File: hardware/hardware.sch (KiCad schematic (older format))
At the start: 32 parts, among them J1 6P6C, J2 RJ45_LED_Shielded, Q1 BUK7M33-60EX, U1 Teensy4.1_DEV-16771, U2 LT1910, U3 OKI, U4 OKI-78SR-3.3_1.5-W36H-C, U5 OPAMP

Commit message: Footprints and layout work
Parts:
- C10, C11, C12, C13, C14, C15: footprint (none) -> Capacitor_SMD:C_0603_1608Metric_Pad1.08x0.95mm_HandSolder
- J2: footprint (none) -> MRDT_Connectors:RJ45_Teensy
- R2, R3, R4, R5: footprint (none) -> Resistor_SMD:R_0603_1608Metric_Pad0.98x0.95mm_HandSolder
- U5: footprint (none) -> Package_SO:SOIC-14_3.9x8.7mm_P1.27mm
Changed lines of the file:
@@
 F 0 "J2" V 750 4450 50  0000 L CNN
 F 1 "RJ45_LED_Shielded" V 850 4100 50  0000 L CNN
-F 2 "" V 1350 4575 50  0001 C CNN
+F 2 "MRDT_Connectors:RJ45_Teensy" V 1350 4575 50  0001 C CNN
 F 3 "~" V 1350 4575 50  0001 C CNN
 	1    1350 4550
@@
 F 0 "U5" H 7294 1796 50  0000 L CNN
 F 1 "OPAMP" H 7294 1705 50  0000 L CNN
-F 2 "" H 6950 1750 50  0001 C CNN
+F 2 "Package_SO:SOIC-14_3.9x8.7mm_P1.27mm" H 6950 1750 50  0001 C CNN
 F 3 "~" H 6950 1750 50  0001 C CNN
 	1    6950 1750
@@
 F 0 "R2" V 5893 1650 50  0000 C CNN
 F 1 "R" V 5984 1650 50  0000 C CNN
-F 2 "" V 6030 1650 50  0001 C CNN
+F 2 "Resistor_SMD:R_0603_1608Metric_Pad0.98x0.95mm_HandSolder" V 6030 1650 50  0001 C CNN
 F 3 "~" H 6100 1650 50  0001 C CNN
 	1    6100 1650
@@
 F 0 "R3" H 6420 2046 50  0000 L CNN
 F 1 "R" H 6420 1955 50  0000 L CNN
-F 2 "" V 6280 2000 50  0001 C CNN
+F 2 "Resistor_SMD:R_0603_1608Metric_Pad0.98x0.95mm_HandSolder" V 6280 2000 50  0001 C CNN
 F 3 "~" H 6350 2000 50  0001 C CNN
 	1    6350 2000
@@
 F 0 "R4" H 6620 1446 50  0000 L CNN
 F 1 "R" H 6620 1355 50  0000 L CNN
-F 2 "" V 6480 1400 50  0001 C CNN
+F 2 "Resistor_SMD:R_0603_1608Metric_Pad0.98x0.95mm_HandSolder" V 6480 1400 50  0001 C CNN
 F 3 "~" H 6550 1400 50  0001 C CNN
 	1    6550 1400
@@
 F 0 "R5" V 6893 2200 50  0000 C CNN
 F 1 "R" V 6984 2200 50  0000 C CNN
-F 2 "" V 7030 2200 50  0001 C CNN
+F 2 "Resistor_SMD:R_0603_1608Metric_Pad0.98x0.95mm_HandSolder" V 7030 2200 50  0001 C CNN
 F 3 "~" H 7100 2200 50  0001 C CNN
 	1    7100 2200
@@
 F 0 "C10" H 1335 1904 50  0000 R CNN
 F 1 "10uF" H 1335 1995 50  0000 R CNN
-F 2 "" H 1488 1800 50  0001 C CNN
+F 2 "Capacitor_SMD:C_0603_1608Metric_Pad1.08x0.95mm_HandSolder" H 1488 1800 50  0001 C CNN
 F 3 "~" H 1450 1950 50  0001 C CNN
 	1    1450 1950
@@
 F 0 "C13" H 935 1904 50  0000 R CNN
 F 1 "10uF" H 935 1995 50  0000 R CNN
-F 2 "" H 1088 1800 50  0001 C CNN
+F 2 "Capacitor_SMD:C_0603_1608Metric_Pad1.08x0.95mm_HandSolder" H 1088 1800 50  0001 C CNN
 F 3 "~" H 1050 1950 50  0001 C CNN
 	1    1050 1950
@@
 F 0 "C11" H 535 1904 50  0000 R CNN
 F 1 "10uF" H 535 1995 50  0000 R CNN
-F 2 "" H 688 1800 50  0001 C CNN
+F 2 "Capacitor_SMD:C_0603_1608Metric_Pad1.08x0.95mm_HandSolder" H 688 1800 50  0001 C CNN
 F 3 "~" H 650 1950 50  0001 C CNN
 	1    650  1950
@@
 F 0 "C15" H 1335 2304 50  0000 R CNN
 F 1 "10uF" H 1335 2395 50  0000 R CNN
-F 2 "" H 1488 2200 50  0001 C CNN
+F 2 "Capacitor_SMD:C_0603_1608Metric_Pad1.08x0.95mm_HandSolder" H 1488 2200 50  0001 C CNN
 F 3 "~" H 1450 2350 50  0001 C CNN
 	1    1450 2350
@@
 F 0 "C14" H 935 2304 50  0000 R CNN
 F 1 "10uF" H 935 2395 50  0000 R CNN
-F 2 "" H 1088 2200 50  0001 C CNN
+F 2 "Capacitor_SMD:C_0603_1608Metric_Pad1.08x0.95mm_HandSolder" H 1088 2200 50  0001 C CNN
 F 3 "~" H 1050 2350 50  0001 C CNN
 	1    1050 2350
@@
 F 0 "C12" H 535 2304 50  0000 R CNN
 F 1 "10uF" H 535 2395 50  0000 R CNN
-F 2 "" H 688 2200 50  0001 C CNN
+F 2 "Capacitor_SMD:C_0603_1608Metric_Pad1.08x0.95mm_HandSolder" H 688 2200 50  0001 C CNN
 F 3 "~" H 650 2350 50  0001 C CNN
 	1    650  2350
@@
 Parallel = Sum
 $Comp
-L power:+12VA #PWR?
+L power:+12VA #PWR0102
 U 1 1 6191BFFF
 P 1050 2700
-F 0 "#PWR?" H 1050 2550 50  0001 C CNN
+F 0 "#PWR0102" H 1050 2550 50  0001 C CNN
 F 1 "+12VA" H 1065 2873 50  0000 C CNN
 F 2 "" H 1050 2700 50  0001 C CNN
@@
 $EndComp
 $Comp
-L power:+3V3 #PWR?
+L power:+3V3 #PWR0103
 U 1 1 6188A195
 P 5800 1150
-F 0 "#PWR?" H 5800 1000 50  0001 C CNN
+F 0 "#PWR0103" H 5800 1000 50  0001 C CNN
 F 1 "+3V3" H 5815 1323 50  0000 C CNN
 F 2 "" H 5800 1150 50  0001 C CNN
@@
 $EndComp
 $Comp
-L power:+3V3 #PWR?
+L power:+3V3 #PWR0104
 U 1 1 6188AFC9
 P 6850 1300
-F 0 "#PWR?" H 6850 1150 50  0001 C CNN
+F 0 "#PWR0104" H 6850 1150 50  0001 C CNN
 F 1 "+3V3" H 6865 1473 50  0000 C CNN
 F 2 "" H 6850 1300 50  0001 C CNN

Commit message: Added more mosfets and sensors
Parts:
- removed C1: 0.1uF, Capacitor_SMD:C_0603_1608Metric_Pad1.08x0.95mm_HandSolder, symbol Device:C
- removed C2: 10uF 50V, Capacitor_SMD:C_0603_1608Metric_Pad1.08x0.95mm_HandSolder, symbol Device:CP1
- removed Conn2: Molex_uF_S_02, MRDT_Connectors:MOLEX_uF_S_02_Horizontal, symbol MRDT_Connectors:Molex_uF_S_02
- removed Q1: BUK7M33-60EX, Package_TO_SOT_SMD:LFPAK33, symbol Transistor_FET:BUK7M33-60EX
- removed R1: 5.1k, Resistor_SMD:R_0603_1608Metric_Pad0.98x0.95mm_HandSolder, symbol Device:R
- removed R2, R3, R4, R5: R, Resistor_SMD:R_0603_1608Metric_Pad0.98x0.95mm_HandSolder, symbol Device:R
- removed TP1, TP2: TestPoint, symbol Connector:TestPoint
- removed U2: LT1910, Package_SO:SOIC-8-N7_3.9x4.9mm_P1.27mm, symbol hardware-rescue:LT1910-MRDT_ICs
- removed U5: OPAMP, Package_SO:SOIC-14_3.9x8.7mm_P1.27mm, symbol pspice:OPAMP
- U1: footprint MRDT_Shields:MODULE_DEV-16771 -> MRDT_Shields:Teensy_4_1_Vertical
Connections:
- wire segments 144 -> 108
- no-connect marks 56 -> 52
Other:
- note removed: "Gate Driver"
- note removed: "MOSFET"
- note removed: "R2 = R4\nR3 = R5\nVout = (R3/R2)(V1-V2)"
- note removed: "Test points will change\nto something else"
- note removed: "Thermistor"
- moved on the sheet: C10, C11, C12, C13, C14, C15, C3, C4, C5, C7, C8, C9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

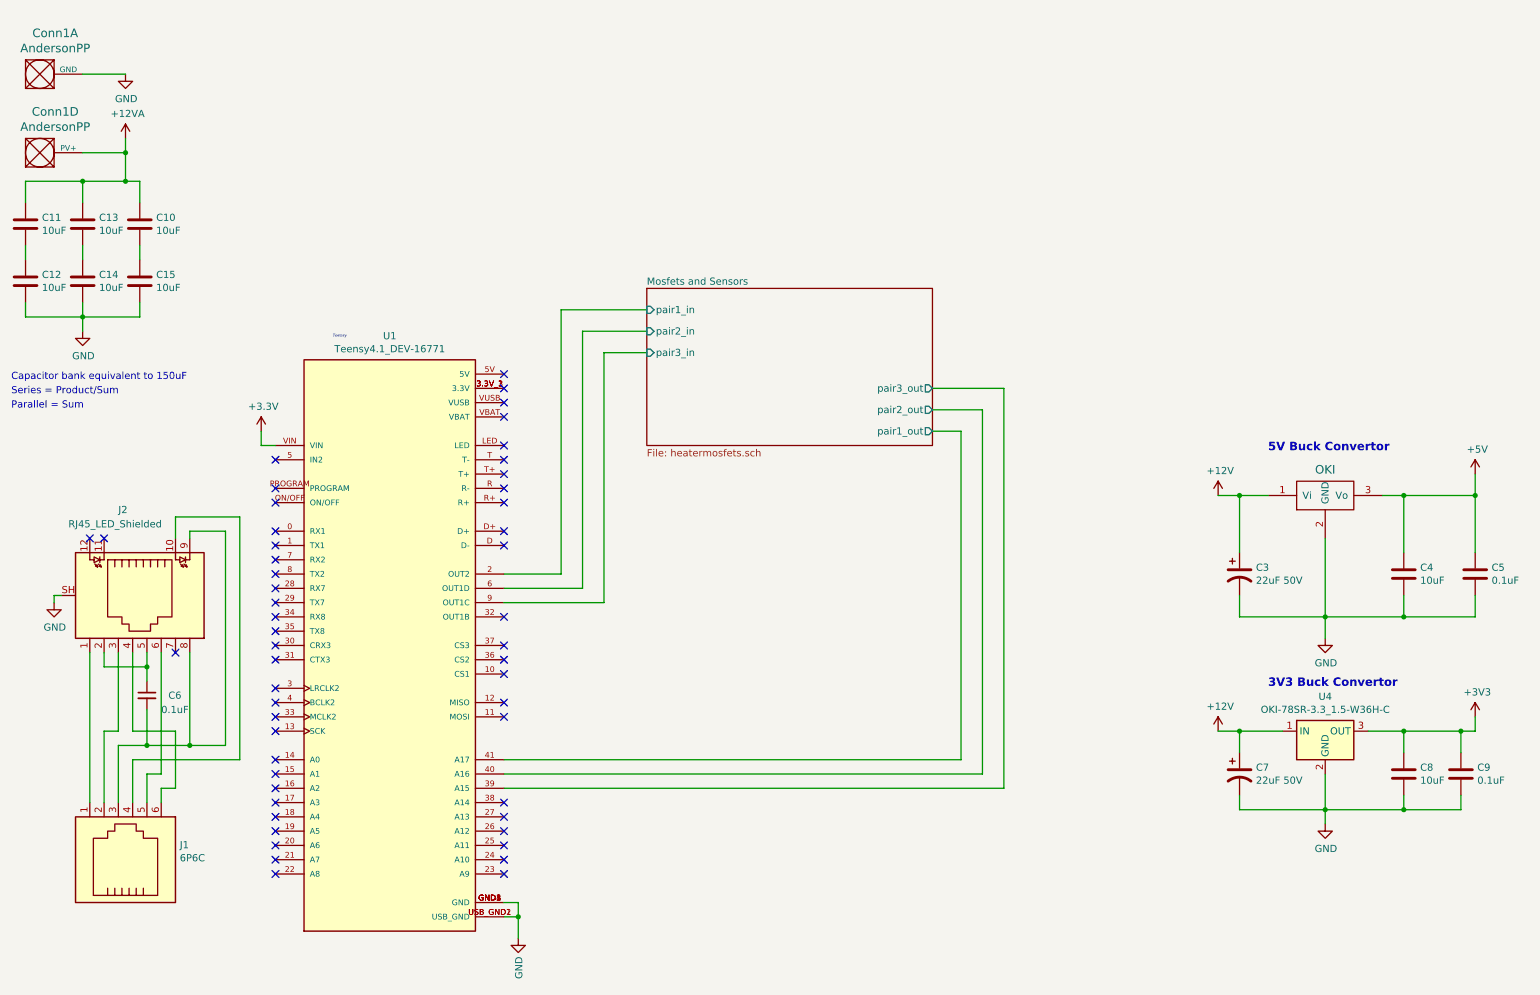
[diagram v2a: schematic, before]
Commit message: Capbank and breakout thermistor
Redid the capacitor bank and added a copy of the sheet with thermistors so we can change to other sensors for now. Also made some aesthetic changes.
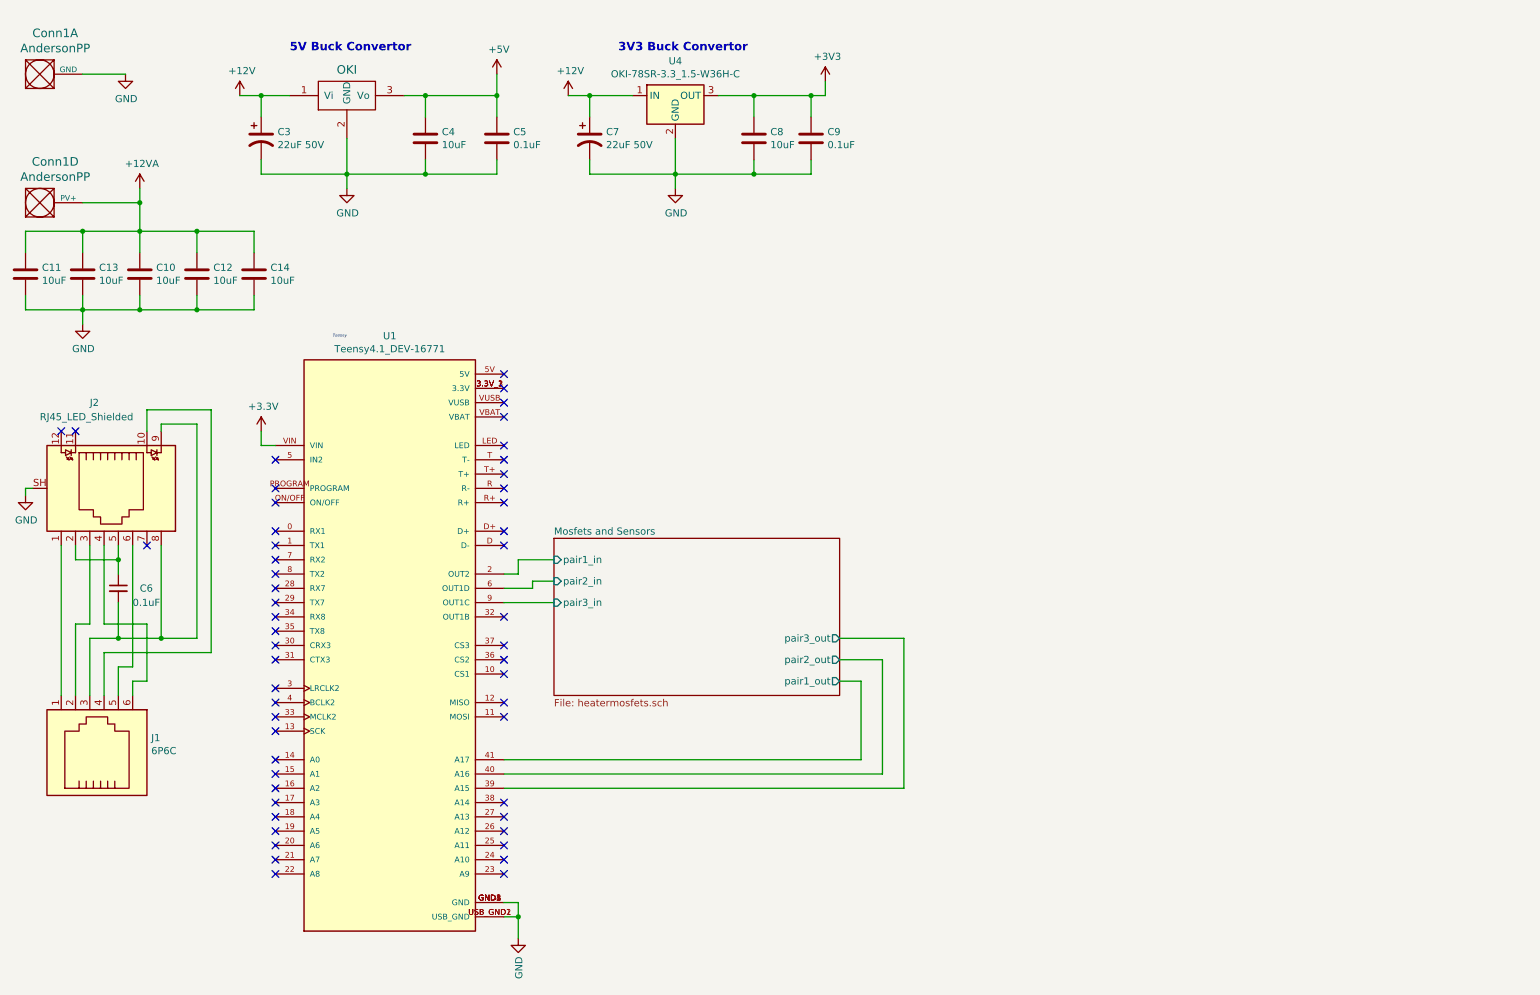
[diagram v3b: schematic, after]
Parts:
- removed C15: 10uF, Capacitor_SMD:C_0603_1608Metric_Pad1.08x0.95mm_HandSolder, symbol Device:C
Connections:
- net +12VA: now also C12.2, C14.2
- net GND: now also C10.1, C11.1, C13.1
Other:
- note removed: "Capacitor bank equivalent to 150uF"
- note removed: "Parallel = Sum"
- note removed: "Series = Product/Sum"
- moved on the sheet: C10, C11, C13, C3, C4, C5, C6, C7, C8, C9, Conn1D, J1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

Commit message: Updated Andersons and layout
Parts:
- removed C10, C11, C12, C13, C14: 10uF, Capacitor_SMD:C_0603_1608Metric_Pad1.08x0.95mm_HandSolder, symbol Device:C
- removed unit 4 of Conn1
- added unit 2 of Conn2
- added unit 3 of Conn2
- Conn2: renamed from Conn1; footprint MRDT_Connectors:Anderson_1_Horizontal -> MRDT_Connectors:Anderson_3_Horizontal_Side_by_Side
- J1: footprint (none) -> Connector_PinHeader_2.00mm:PinHeader_2x03_P2.00mm_Vertical
- renumbered C6 to C1, C3 to C2, C4 to C3, C5 to C4, C7 to C5, C8 to C6, C9 to C7, U3 to U1, U1 to U2, U4 to U3
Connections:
- net +12V: now also Conn2.2 (V+Log)
- net +12VA: now also Conn2.3 (V+Act)
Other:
- moved on the sheet: C1, J1, J2, U2

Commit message: CDR Changes
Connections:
- net +3V3: now also U2.3.3V_1 (3.3V), U2.3.3V_2 (3.3V), U2.3.3V_3 (3.3V); no longer U2.VIN
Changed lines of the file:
@@
 Wire Wire Line
 	1200 900  1000 900
-NoConn ~ 3900 2400
 NoConn ~ 3900 2500
 NoConn ~ 3900 2600
@@
 NoConn ~ 3900 2300
 Wire Wire Line
-	2200 2700 2200 2800
-Wire Wire Line
-	2200 2800 2300 2800
-Wire Wire Line
 	3900 6100 4000 6100
 Wire Wire Line
@@
 	5450 1050 5700 1050
 NoConn ~ 2300 5000
-$Comp
-L hardware-rescue:Teensy4.1_DEV-16771-MRDT_Shields U2
-U 1 1 6158A854
-P 3100 4200
-F 0 "U2" H 3100 6367 50  0000 C CNN
-F 1 "Teensy4.1_DEV-16771" H 3100 6276 50  0000 C CNN
-F 2 "MRDT_Shields:Teensy_4_1_Vertical" H 5200 3900 50  0001 L BNN
-F 3 "" H 3100 4200 50  0001 L BNN
-F 4 "Manufacturer recommendations" H 5200 3650 50  0001 L BNN "STANDARD"
-F 5 "4.07mm" H 5450 3450 50  0001 L BNN "MAXIMUM_PACKAGE_HEIGHT"
-F 6 "SparkFun Electronics" H 5400 3300 50  0001 L BNN "MANUFACTURER"
-F 7 "4.1" H 2800 2000 50  0001 L BNN "PARTREV"
-	1    3100 4200
-	1    0    0    -1
-$EndComp
 $Comp
 L Connector:RJ45_LED_Shielded J2
@@
 L power:+3.3V #PWR06
 U 1 1 617FDF47
-P 2200 2700
-F 0 "#PWR06" H 2200 2550 50  0001 C CNN
-F 1 "+3.3V" H 2215 2873 50  0000 C CNN
-F 2 "" H 2200 2700 50  0001 C CNN
-F 3 "" H 2200 2700 50  0001 C CNN
-	1    2200 2700
+P 4000 2350
+F 0 "#PWR06" H 4000 2200 50  0001 C CNN
+F 1 "+3.3V" H 4015 2523 50  0000 C CNN
+F 2 "" H 4000 2350 50  0001 C CNN
+F 3 "" H 4000 2350 50  0001 C CNN
+	1    4000 2350
 	1    0    0    -1
 $EndComp
@@
 	1    0    0    -1
 $EndComp
+$Comp
+L hardware-rescue:Teensy4.1_DEV-16771-MRDT_Shields U2
+U 1 1 6158A854
+P 3100 4200
+F 0 "U2" H 3100 6367 50  0000 C CNN
+F 1 "Teensy4.1_DEV-16771" H 3100 6276 50  0000 C CNN
+F 2 "MRDT_Shields:Teensy_4_1_Vertical" H 5200 3900 50  0001 L BNN
+F 3 "" H 3100 4200 50  0001 L BNN
+F 4 "Manufacturer recommendations" H 5200 3650 50  0001 L BNN "STANDARD"
+F 5 "4.07mm" H 5450 3450 50  0001 L BNN "MAXIMUM_PACKAGE_HEIGHT"
+F 6 "SparkFun Electronics" H 5400 3300 50  0001 L BNN "MANUFACTURER"
+F 7 "4.1" H 2800 2000 50  0001 L BNN "PARTREV"
+	1    3100 4200
+	1    0    0    -1
+$EndComp
+NoConn ~ 2300 2800
+Wire Wire Line
+	4000 2350 4000 2400
+Wire Wire Line
+	4000 2400 3900 2400
 $EndSCHEMATC

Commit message: Fixed rescue library
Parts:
- Conn2: symbol hardware-rescue:AndersonPP-MRDT_Connectors -> MRDT_Connectors:AndersonPP
- U1: symbol hardware-rescue:OKI-MRDT_Devices -> MRDT_Devices:OKI
- U2: symbol hardware-rescue:Teensy4.1_DEV-16771-MRDT_Shields -> MRDT_Shields:Teensy4.1_DEV-16771
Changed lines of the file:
@@
 $EndDescr
 $Comp
-L hardware-rescue:AndersonPP-MRDT_Connectors Conn2
+L MRDT_Connectors:AndersonPP Conn2
 U 1 1 614D689F
 P 600 1000
@@
 	4000 6000 3900 6000
 $Comp
-L hardware-rescue:OKI-MRDT_Devices U1
+L MRDT_Devices:OKI U1
 U 1 1 615CF578
 P 2650 1150
@@
 $EndComp
 $Comp
-L hardware-rescue:Teensy4.1_DEV-16771-MRDT_Shields U2
+L MRDT_Shields:Teensy4.1_DEV-16771 U2
 U 1 1 6158A854
 P 3100 4200

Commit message: Initial Rev2 Design
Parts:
- added D1, D2, D6, D7, D8, D9: LED, LED_SMD:LED_0603_1608Metric_Pad1.05x0.95mm_HandSolder, symbol Device:LED
- added R4: 1000, Resistor_SMD:R_0603_1608Metric_Pad0.98x0.95mm_HandSolder, symbol Device:R
- added R5: 300, Resistor_SMD:R_0603_1608Metric_Pad0.98x0.95mm_HandSolder, symbol Device:R
- added R6, R7, R8, R9: 120, Resistor_SMD:R_0603_1608Metric_Pad0.98x0.95mm_HandSolder, symbol Device:R
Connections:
- net +12VA: now also R4.2
- net +3V3: now also R6.2
- net +5V: now also R5.2
- net GND: now also D1.1 (K), D2.1 (K), D6.1 (K), D7.1 (K), D8.1 (K), D9.1 (K)
- net at U2.0 (RX1): now also R7.1
- net at U2.1 (TX1): now also R8.1
- net at U2.7 (RX2): now also R9.1
- new net: D1.2 (A), R5.1
- new net: D2.2 (A), R6.1
- new net: D6.2 (A), R7.2
- new net: D7.2 (A), R8.2
- new net: D8.2 (A), R9.2
- new net: D9.2 (A), R4.1
- no-connect marks 52 -> 49
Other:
- moved on the sheet: C5, C6, C7, U3
